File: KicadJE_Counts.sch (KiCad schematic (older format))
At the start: 17 parts, among them J101 In7, J102 In6, J103 In3, J104 Out10, J105 Out11, J106 Out9, J107 Out6

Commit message: Update KicadJE_Counts.sch
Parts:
- gave numbers to parts that had none: 4
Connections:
- net +12V: no longer R108.2
- new net +12Vc: R108.2
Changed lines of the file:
@@
 P 10550 1650
 AR Path="/5D60ED9A/5ECDBE01" Ref="D?"  Part="1"
-AR Path="/5ECDBE01" Ref="D?"  Part="1"
-F 0 "D?" V 10589 1532 50  0000 R CNN
+AR Path="/5ECDBE01" Ref="D102"  Part="1"
+F 0 "D102" V 10589 1532 50  0000 R CNN
 F 1 "D_LED" V 10498 1532 50  0000 R CNN
 F 2 "AJ:LED_0805_2012Metric_Pad1.15x1.40mm_HandSolder" H 10550 1650 50  0001 C CNN
@@
 AR Path="/5D4DB615/5ECDBE07" Ref="R?"  Part="1"
 AR Path="/5D60ED9A/5ECDBE07" Ref="R?"  Part="1"
-AR Path="/5ECDBE07" Ref="R?"  Part="1"
-F 0 "R?" V 10550 1275 50  0000 C CNN
+AR Path="/5ECDBE07" Ref="R108"  Part="1"
+F 0 "R108" V 10550 1275 50  0000 C CNN
 F 1 "DNP" V 10475 1250 50  0000 C CNN
 F 2 "AJ:R_0805_AJ" V 10480 1275 50  0001 C CNN
@@
 	-1   0    0    1
 $EndComp
-Text GLabel 10550 1075 1    50   Input ~ 0
-+12V
 $Comp
-L power:GND #PWR?
+L power:GND #PWR0103
 U 1 1 5ECDBE0E
 P 10550 1900
-AR Path="/5ECDBE0E" Ref="#PWR?"  Part="1"
+AR Path="/5ECDBE0E" Ref="#PWR0103"  Part="1"
 AR Path="/5D60ED9A/5ECDBE0E" Ref="#PWR?"  Part="1"
-F 0 "#PWR?" H 10550 1650 50  0001 C CNN
+F 0 "#PWR0103" H 10550 1650 50  0001 C CNN
 F 1 "GND" H 10555 1727 50  0000 C CNN
 F 2 "" H 10550 1900 50  0001 C CNN
@@
 P 10175 1650
 AR Path="/5D60ED9A/5ECDC753" Ref="D?"  Part="1"
-AR Path="/5ECDC753" Ref="D?"  Part="1"
-F 0 "D?" V 10214 1532 50  0000 R CNN
+AR Path="/5ECDC753" Ref="D101"  Part="1"
+F 0 "D101" V 10214 1532 50  0000 R CNN
 F 1 "D_LED" V 10123 1532 50  0000 R CNN
 F 2 "AJ:LED_0805_2012Metric_Pad1.15x1.40mm_HandSolder" H 10175 1650 50  0001 C CNN
@@
 AR Path="/5D4DB615/5ECDC75D" Ref="R?"  Part="1"
 AR Path="/5D60ED9A/5ECDC75D" Ref="R?"  Part="1"
-AR Path="/5ECDC75D" Ref="R?"  Part="1"
-F 0 "R?" V 10175 1275 50  0000 C CNN
+AR Path="/5ECDC75D" Ref="R107"  Part="1"
+F 0 "R107" V 10175 1275 50  0000 C CNN
 F 1 "DNP" V 10100 1250 50  0000 C CNN
 F 2 "AJ:R_0805_AJ" V 10105 1275 50  0001 C CNN
@@
 +12V
 $Comp
-L power:GND #PWR?
+L power:GND #PWR0102
 U 1 1 5ECDC768
 P 10175 1900
-AR Path="/5ECDC768" Ref="#PWR?"  Part="1"
+AR Path="/5ECDC768" Ref="#PWR0102"  Part="1"
 AR Path="/5D60ED9A/5ECDC768" Ref="#PWR?"  Part="1"
-F 0 "#PWR?" H 10175 1650 50  0001 C CNN
+F 0 "#PWR0102" H 10175 1650 50  0001 C CNN
 F 1 "GND" H 10180 1727 50  0000 C CNN
 F 2 "" H 10175 1900 50  0001 C CNN
@@
 Wire Wire Line
 	10175 1125 10175 1075
+Text GLabel 10550 1075 1    50   Input ~ 0
++12Vc
 $EndSCHEMATC

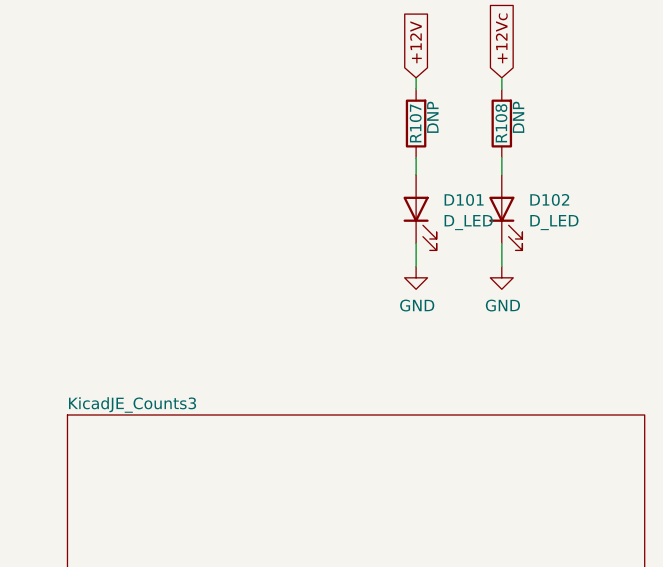
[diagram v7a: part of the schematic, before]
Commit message: Update KicadJE_Counts.sch
GND conn
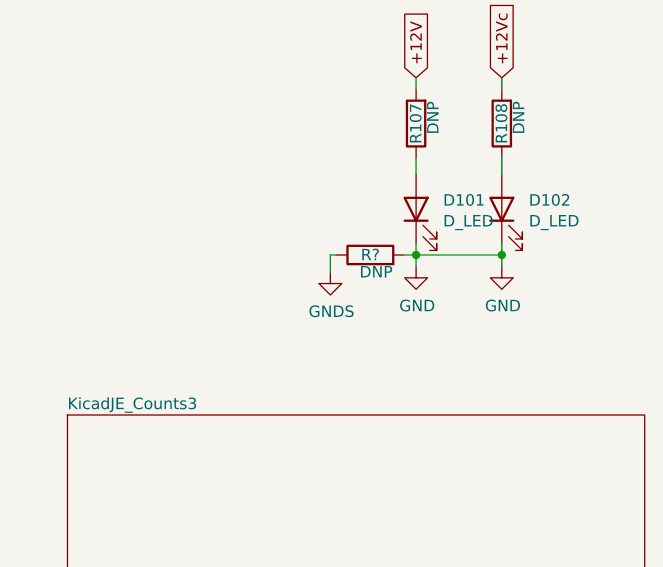
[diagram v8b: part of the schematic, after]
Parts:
- added R?: DNP, AJ:R_0805_AJ, symbol Device:R
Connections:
- net GND: now also R?.2
- new net GNDS: R?.1
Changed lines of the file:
@@
 $EndComp
 Wire Wire Line
-	10550 1900 10550 1800
+	10550 1900 10550 1850
 Wire Wire Line
 	10550 1500 10550 1425
@@
 $EndComp
 Wire Wire Line
-	10175 1900 10175 1800
+	10175 1900 10175 1850
 Wire Wire Line
 	10175 1500 10175 1425
@@
 Text GLabel 10550 1075 1    50   Input ~ 0
 +12Vc
+$Comp
+L power:GNDS #PWR?
+U 1 1 5ECE79CC
+P 9800 1925
+AR Path="/5ECE79CC" Ref="#PWR?"  Part="1"
+AR Path="/5D60ED9A/5ECE79CC" Ref="#PWR?"  Part="1"
+AR Path="/5C781441/5ECE79CC" Ref="#PWR?"  Part="1"
+F 0 "#PWR?" H 9800 1675 50  0001 C CNN
+F 1 "GNDS" H 9805 1752 50  0000 C CNN
+F 2 "" H 9800 1925 50  0001 C CNN
+F 3 "" H 9800 1925 50  0001 C CNN
+	1    9800 1925
+	1    0    0    -1
+$EndComp
+Wire Wire Line
+	9800 1850 9800 1925
+$Comp
+L Device:R R?
+U 1 1 5ECE8C8F
+P 9975 1850
+AR Path="/5CF11B19/5ECE8C8F" Ref="R?"  Part="1"
+AR Path="/5D4DB615/5ECE8C8F" Ref="R?"  Part="1"
+AR Path="/5D60ED9A/5ECE8C8F" Ref="R?"  Part="1"
+AR Path="/5ECE8C8F" Ref="R?"  Part="1"
+F 0 "R?" V 9975 1850 50  0000 C CNN
+F 1 "DNP" V 9900 1825 50  0000 C CNN
+F 2 "AJ:R_0805_AJ" V 9905 1850 50  0001 C CNN
+F 3 "~" H 9975 1850 50  0001 C CNN
+	1    9975 1850
+	0    -1   -1   0
+$EndComp
+Wire Wire Line
+	9800 1850 9825 1850
+Connection ~ 10550 1850
+Wire Wire Line
+	10550 1850 10550 1800
+Wire Wire Line
+	10125 1850 10175 1850
+Connection ~ 10175 1850
+Wire Wire Line
+	10175 1850 10175 1800
+Wire Wire Line
+	10175 1850 10550 1850
 $EndSCHEMATC
